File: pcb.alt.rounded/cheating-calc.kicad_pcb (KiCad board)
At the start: 2 copper layers, 72 x 22 mm, 8 parts, among them J1 Conn_01x04, Q1 MMBF170, Q2 MMBF170, U1 XIAO-ESP32-S3-SMD

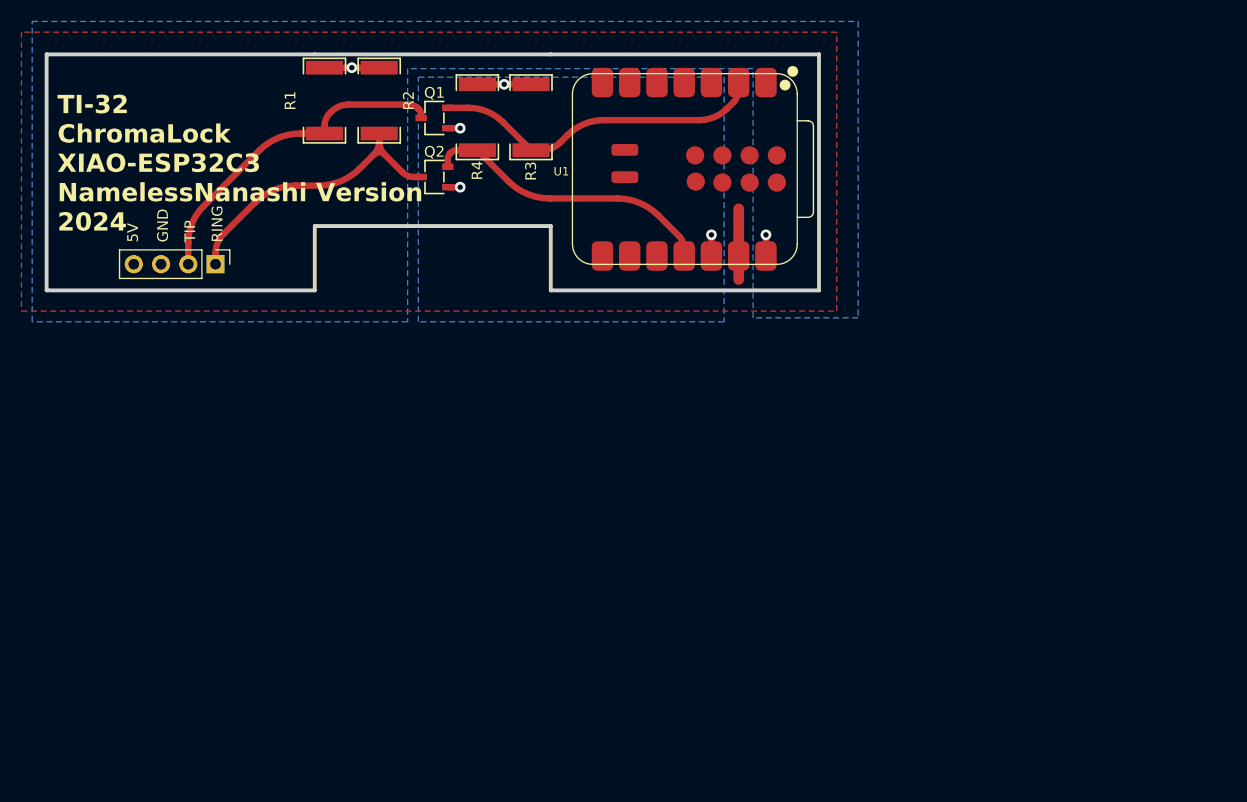
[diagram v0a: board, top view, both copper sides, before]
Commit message: tweak silkscreen and schematic
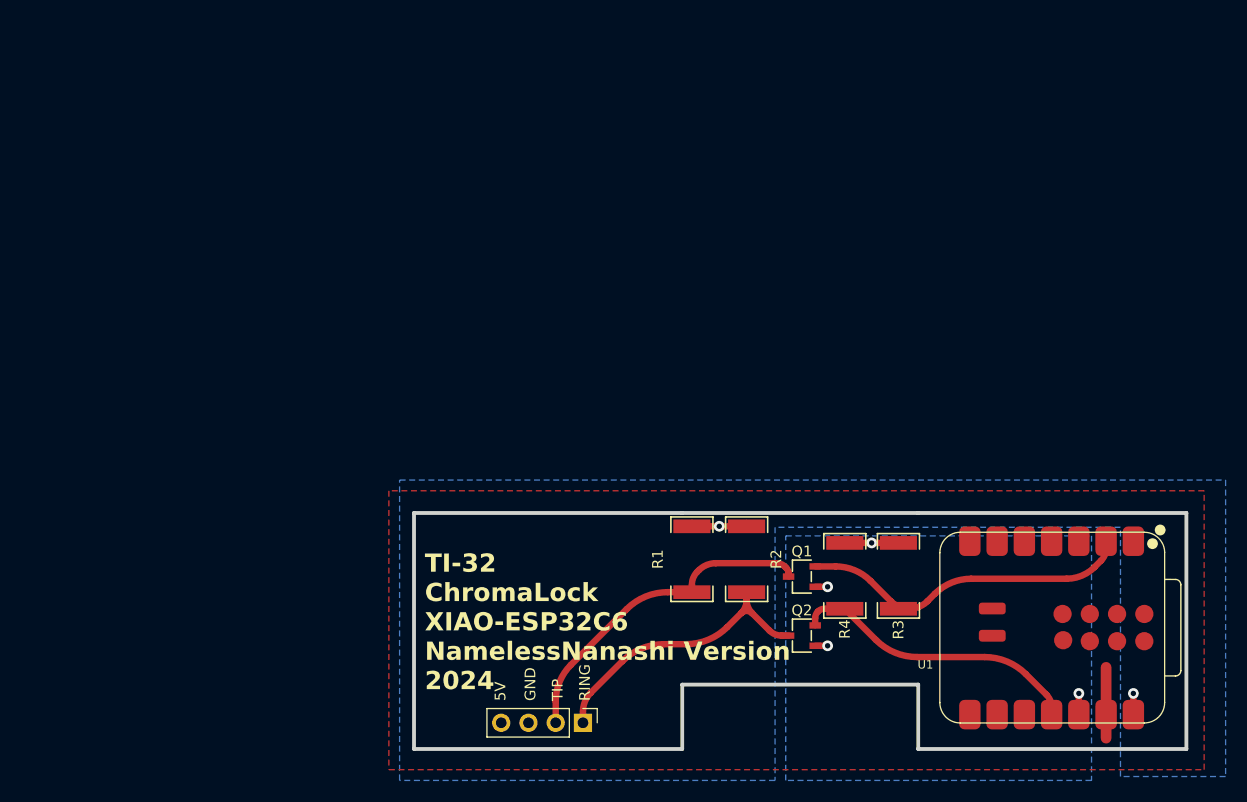
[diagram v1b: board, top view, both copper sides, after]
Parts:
- U1: value XIAO-ESP32-S3-SMD -> XIAO-ESP32-C6-SMD
- moved J1 54.8 mm to (135.3, 114.4)
- moved R3 54.8 mm to (164.8, 100.7)
- moved R4 54.8 mm to (159.8, 100.7)
- moved Q1 54.8 mm to (155.8, 100.8)
- moved Q2 54.8 mm to (155.8, 106.2)
- moved U1 54.8 mm to (168.5, 96.6)
- moved R1 54.8 mm to (145.5, 99.1)
- moved R2 54.8 mm to (150.6, 99.1)
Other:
- board text added: "TI-32 ChromaLock XIAO-ESP32C6 NamelessNanashi Version 2024"
- board text removed: "TI-32 ChromaLock XIAO-ESP32C3 NamelessNanashi Version 2024"
